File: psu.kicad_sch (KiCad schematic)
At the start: 21 parts, among them U6 TPS7A8001DRBR, U7 TPS7A8001DRBR

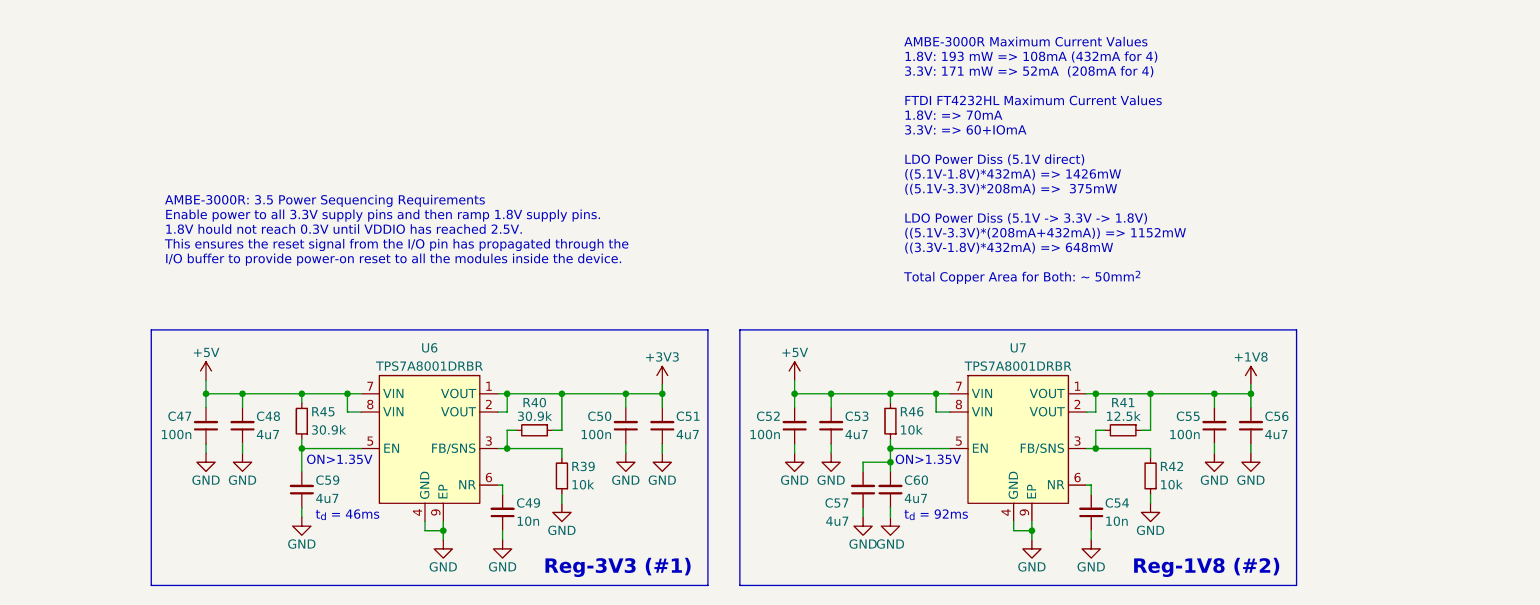
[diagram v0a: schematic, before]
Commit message: Added the AMBE-3000F
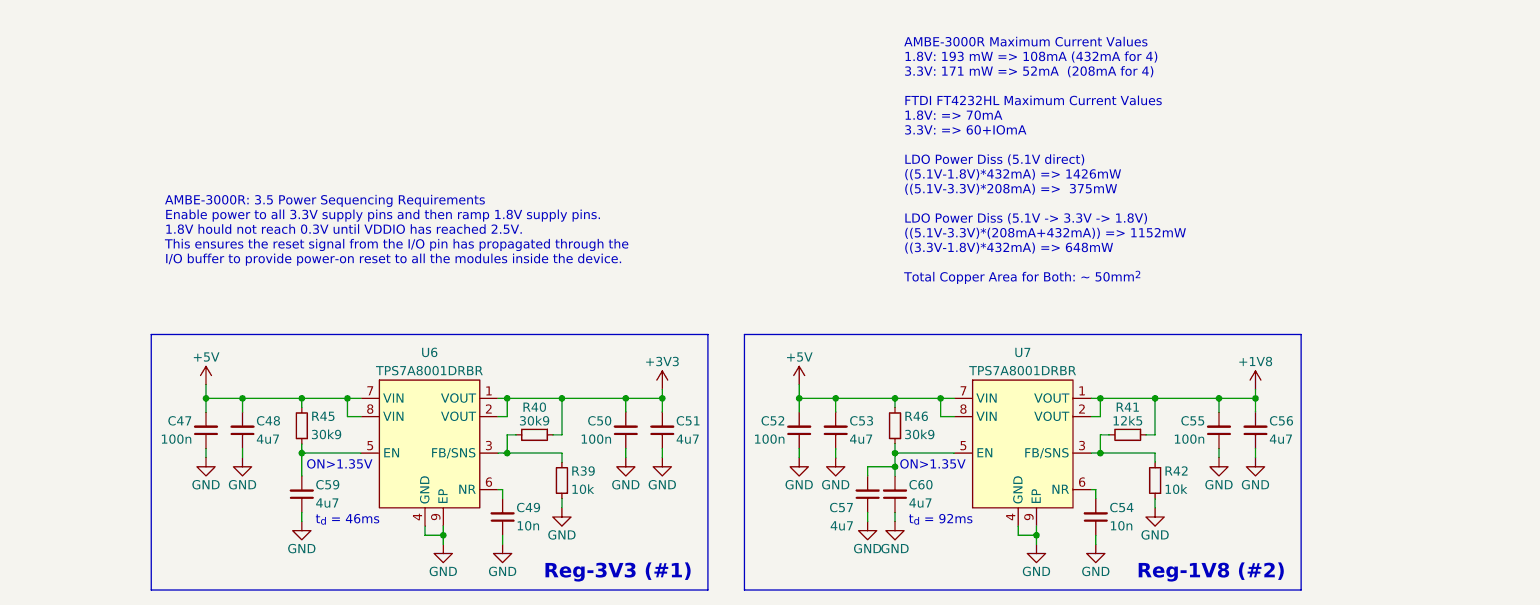
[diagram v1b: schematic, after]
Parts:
- R40, R45: value 30.9k -> 30k9
- R41: value 12.5k -> 12k5
- R46: value 10k -> 30k9
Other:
- moved on the sheet: C47, C48, C49, C50, C51, C52, C53, C54, C55, C56, C57, C59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

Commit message: Schematic V1 done
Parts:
- C21: renamed from C47; footprint (none) -> Capacitor_SMD:C_0603_1608Metric
- C22: renamed from C48; footprint (none) -> Capacitor_SMD:C_0603_1608Metric
- C23: renamed from C59; footprint (none) -> Capacitor_SMD:C_0603_1608Metric
- C24: renamed from C49; footprint (none) -> Capacitor_SMD:C_0603_1608Metric
- C25: renamed from C50; footprint (none) -> Capacitor_SMD:C_0603_1608Metric
- C26: renamed from C51; footprint (none) -> Capacitor_SMD:C_0603_1608Metric
- C27: renamed from C52; footprint (none) -> Capacitor_SMD:C_0603_1608Metric
- C28: renamed from C53; footprint (none) -> Capacitor_SMD:C_0603_1608Metric
- C29: renamed from C57; footprint (none) -> Capacitor_SMD:C_0603_1608Metric
- C30: renamed from C60; footprint (none) -> Capacitor_SMD:C_0603_1608Metric
- C31: renamed from C54; footprint (none) -> Capacitor_SMD:C_0603_1608Metric
- C32: renamed from C55; footprint (none) -> Capacitor_SMD:C_0603_1608Metric
- C33: renamed from C56; footprint (none) -> Capacitor_SMD:C_0603_1608Metric
- R24: renamed from R45; footprint (none) -> Resistor_SMD:R_0603_1608Metric
- R25: renamed from R40; footprint (none) -> Resistor_SMD:R_0603_1608Metric
- R26: renamed from R39; footprint (none) -> Resistor_SMD:R_0603_1608Metric
- R27: renamed from R46; footprint (none) -> Resistor_SMD:R_0603_1608Metric
- R28: renamed from R41; footprint (none) -> Resistor_SMD:R_0603_1608Metric
- R29: renamed from R42; footprint (none) -> Resistor_SMD:R_0603_1608Metric
- renumbered U6 to U5, U7 to U6
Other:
- company: (none) -> M1GEO & G8OCV
- title: (none) -> Quad AMBE-3000R Board

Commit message: Most of the layout done
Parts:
- renumbered C21 to C20, C22 to C21, C23 to C22, C24 to C23, C25 to C24, C26 to C25, C27 to C26, C28 to C27, C29 to C28, C30 to C29, C31 to C30, C32 to C31, C33 to C32, R24 to R23, R25 to R24, R26 to R25, R27 to R26, R28 to R27, R29 to R28

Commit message: Final updates before manufacture of V1.00
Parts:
- added D9: WHT, LED_SMD:LED_0603_1608Metric, symbol Device:LED
- added Q5: AO3400A, Package_TO_SOT_SMD:SOT-23, symbol Transistor_FET:AO3400A
- added R49: 330R, Resistor_SMD:R_0603_1608Metric, symbol Device:R_Small
- C20, C24, C26, C31: LCSC (none) -> C14663
- C21, C22, C25, C27, C28, C29, C32: LCSC (none) -> C19666
- C23, C30: LCSC (none) -> C57112
- R23, R24, R26: LCSC (none) -> C217957
- R25: LCSC (none) -> C25804
- R27: value 12k5 -> 15k; LCSC (none) -> C22809
- R28: value 10k -> 12k; LCSC (none) -> C22790
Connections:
- net +1V8: now also Q5.1 (G)
- net +3V3: now also R49.1
- net GND: now also R28.2, Q5.2 (S); no longer R28.1
- net at R27.2, U6.3 (FB/SNS): now also R28.1; no longer R28.2
- new net: D9.1 (K), Q5.3 (D)
- new net: D9.2 (A), R49.2
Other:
- note added: "V_{GS(th)}<1.45V Both 3V3 and 1V8 needed to light power LED."
- title: Quad AMBE-3000R Board -> Quad AMBE-3000R Board (Power Supplies & Sequencing)
- moved on the sheet: C20, C21, C22, C23, C24, C25, C26, C27, C28, C29, C30, C31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
